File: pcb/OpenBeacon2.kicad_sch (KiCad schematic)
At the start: 69 parts, among them J1 SMA, J2 SMA CLKIN, J3 BNC, J4 Bias V, J5 GND, Q1 AO3407A, Q2 2N7002, Q3 BS170, Q4 BS170, U1 TPS61085DGKR, U2 25.000 MHz TCXO, U3 SI5351C-B-GMR, U4 INA193AIDBVR, U5 SN74LVC1G17, U6 MCP4725A1T-E/CH

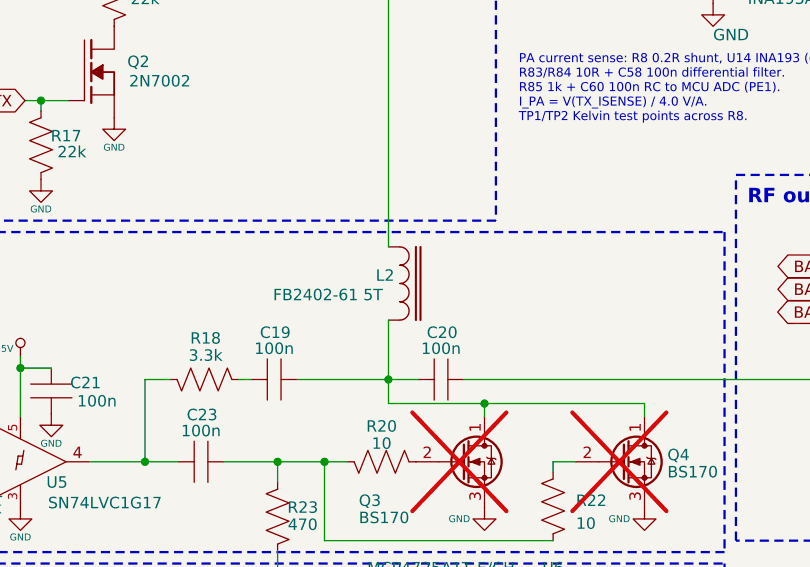
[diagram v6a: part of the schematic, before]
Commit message: L2: mark DNP, source FB2402-61 core from Kits and Parts (drop LCSC C6078003)
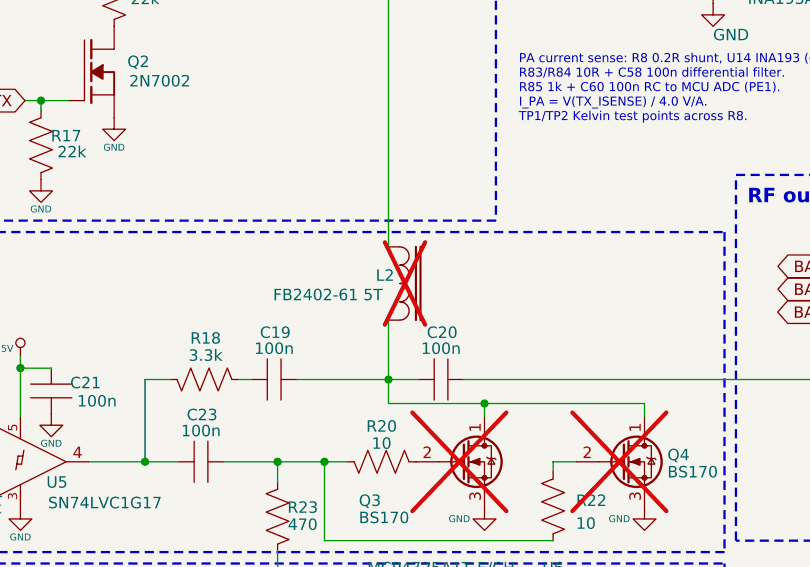
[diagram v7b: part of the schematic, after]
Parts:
- L2: LCSC C6078003 -> (none); Supplier (none) -> Kits and Parts (kitsandparts.com); now not fitted
- Q3: Assembly Hand solder - exclude from JLC assembly -> Hand-wound - exclude from JLC assembly
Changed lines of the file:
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@@
 			)
 		)
-		(property "Assembly" "Hand solder - exclude from JLC assembly"
+		(property "Assembly" "Hand-wound - exclude from JLC assembly"
 			(at 85.09 133.985 0)
 			(effects
@@
 		(on_board yes)
 		(in_pos_files no)
-		(dnp no)
+		(dnp yes)
 		(property "Reference" "L2"
 			(at 88.011 108.966 0)
@@
 			)
 		)
-		(property "LCSC" "C6078003"
+		(property "Supplier" "Kits and Parts (kitsandparts.com)"
 			(at 88.011 108.966 0)
 			(effects
